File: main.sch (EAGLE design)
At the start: 74 parts, among them IC10 FGPMMOPA6H, IC2 25LC1024-I/P, IC6 MPL3115A2LGA, IC7 FXAS21000, IC8 ADXL343BCCZ, Q1 12MHz, Q2 MCP9700A-E/TO, Q3 FQP7P06, Q4 MCP9700A-E/TO, U1 ATMEGA1284P-PU, U2 LT3570EFEPBF, U3 TL431BQLP, X1 132134RP

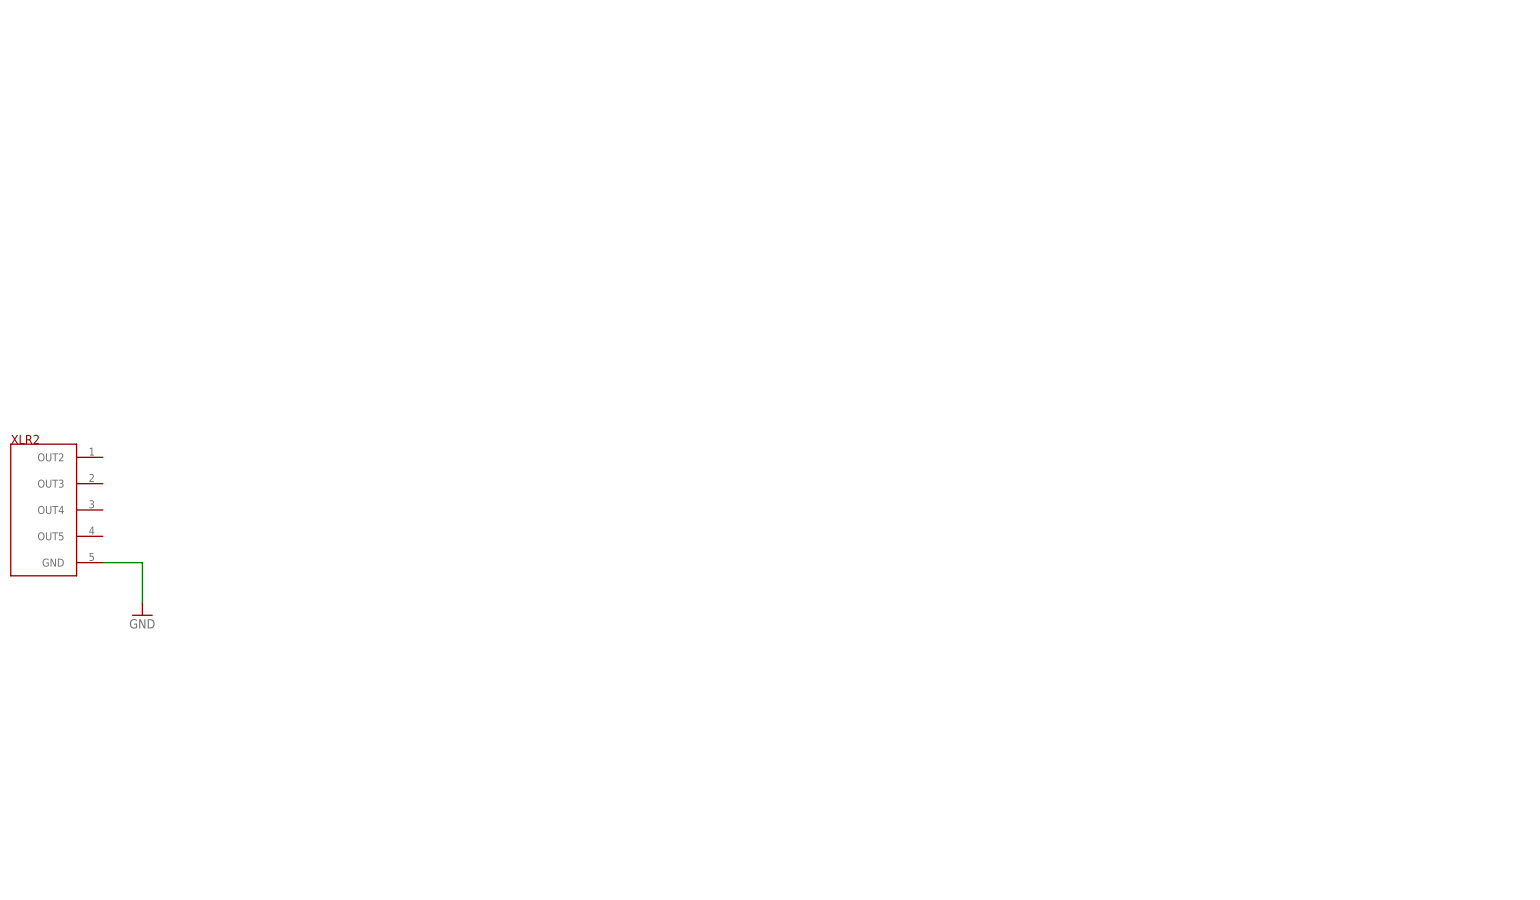
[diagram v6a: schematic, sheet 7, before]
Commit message: Finished Power bank
Finished Power bank.
To do:
Key switch
Short circuit protection (PTCs)
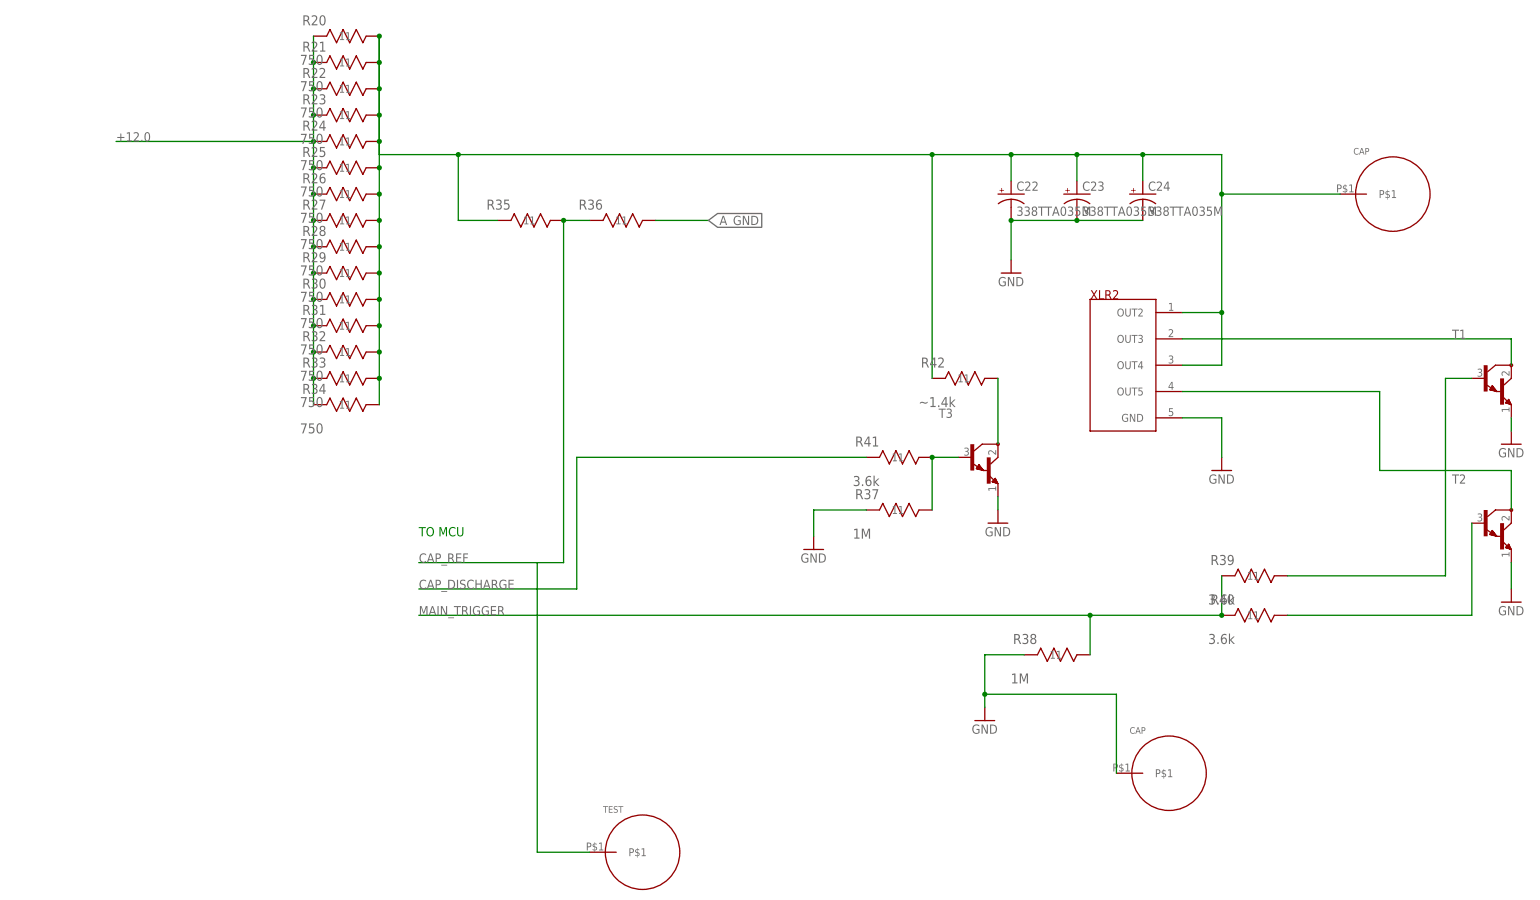
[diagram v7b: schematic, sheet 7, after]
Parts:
- added C22, C23, C24: 338TTA035M, Power:338TTA035M
- added R20, R21, R22, R23, R24, R25, R26, R27, R28, R29, R30, R31, R32, R33, R34: 750, Power:MFR-25FBF52-3K65
- added R35, R36: (no value), Power:MFR-25FBF52-3K65
- added R37, R38: 1M, Power:MFR-25FBF52-3K65
- added R39, R40, R41: 3.6k, Power:MFR-25FBF52-3K65
- added R42: ~1.4k, Power:MFR-25FBF52-3K65
- added T1, T2, T3: (no value), Power:-NPN_DARL-
- added U$1: +3.3V, Power:TEST
- added U$10, U$9: TEST, Power:TEST
- added U$2: +24V, Power:TEST
- added U$3, U$6: BAT+, Power:TEST
- added U$4, U$5: CAP, Power:TEST
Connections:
- new net CAP_DISCHARGE: R41.11, U1.PD4
- new net CAP_REF: R35.22, R36.11, U$9.P$1, U1.PA0
- new net N$75: R42.22, T3.C
- new net N$77: T1.C, XLR2.OUT3
- new net N$78: T2.C, XLR2.OUT5
- new net N$79: R39.22, T1.B
- new net N$80: R40.22, T2.B
- new net N$81: C22.+, C23.+, C24.+, R20.22, R21.22, R22.22, R23.22, R24.22, R25.22, R26.22, R27.22, R28.22, R29.22, R30.22, R31.22, R32.22, R33.22, R34.22, R35.11, R42.11, U$4.P$1, XLR2.OUT2, XLR2.OUT4
- new net N$82: R37.22, R41.22, T3.B
- net +12.0: now also R20.11, R21.11, R22.11, R23.11, R24.11, R25.11, R26.11, R27.11, R28.11, R29.11, R30.11, R31.11, R32.11, R33.11, R34.11
- net 12V_ENABLE: now also U$10.P$1
- net A_GND: now also R36.22
- net BAT+: now also U$6.P$1
- net GND: now also C22.-, C23.-, C24.-, R37.11, R38.11, T1.E, T2.E, T3.E, U$5.P$1
- net MAIN_TRIGGER: now also R38.22, R39.11, R40.11
- net N$8: now also U$2.P$1
- net PWR_JUNC: now also U$3.P$1
- net TEMP: now also U1.PA1; no longer U1.PA0
- net TEMP2: now also U1.PA2; no longer U1.PA1
- net VCC: now also U$1.P$1
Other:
- note added: "TO MCU"
- moved on the sheet: XLR2

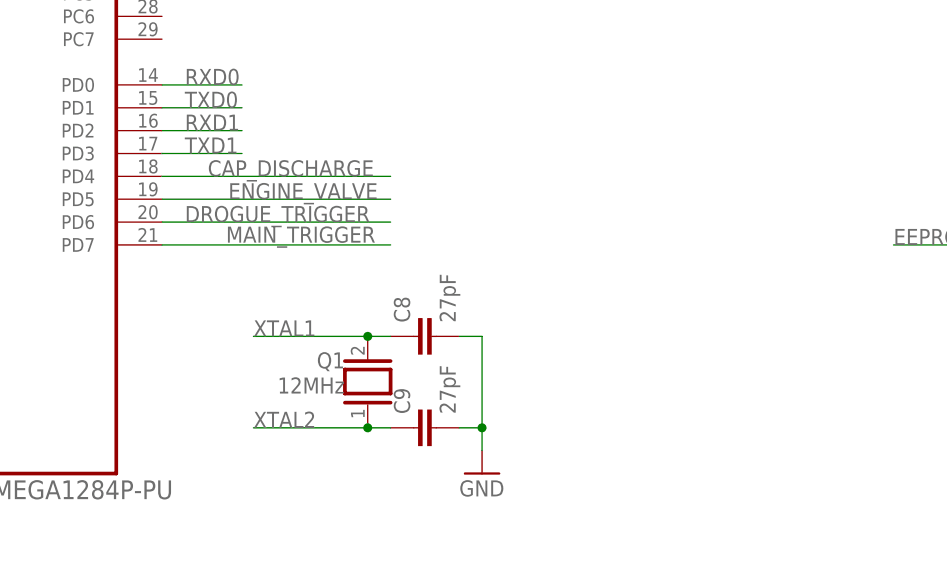
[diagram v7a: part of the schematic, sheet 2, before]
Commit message: Added terminal pads
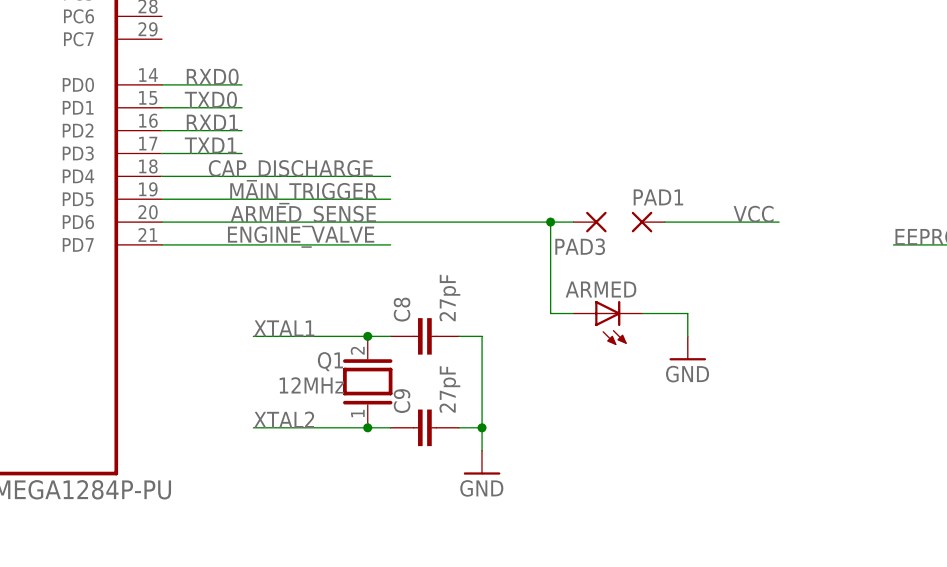
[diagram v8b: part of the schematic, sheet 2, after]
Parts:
- added ARMED: (no value), led:LED5MM
- added PAD1, PAD2, PAD3, PAD6: (no value), Power:CRIMP
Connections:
- removed net DROGUE_TRIGGER: U1.PD6
- new net ARMED_SENSE: ARMED.A, PAD3.P, U1.PD6
- new net N$31: PAD6.P, XLR2.OUT2, XLR2.OUT4
- net ENGINE_VALVE: now also U1.PD7; no longer U1.PD5
- net GND: now also ARMED.C
- net MAIN_TRIGGER: now also U1.PD5; no longer U1.PD7
- net N$81: now also PAD2.P; no longer XLR2.OUT2, XLR2.OUT4
- net VCC: now also PAD1.P
